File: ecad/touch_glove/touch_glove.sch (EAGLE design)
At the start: 173 parts, among them Q1 MCH3474 4A/30V, Q2 MCH3474 4A/30V, Q3 MCH3474 4A/30V, Q4 MCH3474 4A/30V, Q5 MCH3474 4A/30V, Q6 MCH3474 4A/30V, SW1 4A/28V, Y1 16 MHz

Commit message: Rev 2: Touch Glove.  Add op amps to flex sensor set 2.
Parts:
- removed ANT1: 2.45GHz, PiB_radio_frequency:ANTENNA_SMD_CHP-2.45GHZ-0.5DBI-3W
- removed D1: 1A/50V, PiB_discrete_semiconductors:DIODE_GENERAL-PURPOSE_SMD_GP_1A-50V
- removed Y1: 16 MHz, PiB:CRYSTAL_ABM3B_16MHZ_18PF
- added ANT: 2.45GHz, PiB_radio_frequency:ANTENNA_SMD_CHP-2.45GHZ-0.5DBI-3W
- added OPAMP1, OPAMP2, OPAMP3: LM358_DFN-EP, PiB_op_amps:LM358_DFN-EP
- added XTAL: 16 MHz, PiB:CRYSTAL_ABM3B_16MHZ_18PF
- C1, C2, C21, C3: value 100uF/16V -> 100uF/10V
- R1, R32, R33, R34, R35, R36, R37, R38, R39, R40, R41, R42, R43, R44, R45, R46, R47, R48: value 10KΩ -> 10K
- R10, R11, R12, R13, R14, R15, R6, R7, R8, R9: value 47K -> 10K; device PiB_resistors:47KΩ_SMD-0402_1/16W-5% -> PiB_resistors:10KΩ_SMD-0402_1/16W-5%
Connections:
- net A0 renamed SIG
- net PB6 renamed LED_RX
- net PB7 renamed LED_TX
- net PD4 renamed S0
- net PD5 renamed S1
- net PD6 renamed S3
- net PD7 renamed S2
- removed net A1: MCU.(ADC1/A1*)PF1
- removed net A2: MCU.(ADC2/DIG2/A2*)PF2
- removed net A3: MCU.(ADC3/DIG4/A3*)PF3
- removed net A4: MCU.(ADC4/TCK/A4*)PF4
- removed net A5: MCU.(ADC5/TMS/A5*)PF5
- removed net A6: MCU.(ADC6/TDO/A6*)PF6
- removed net A7: MCU.(ADC7/TDI/A7*)PF7
- removed net PB4: MCU.(PCINT4/OC2A/D9-PWM9)PB4
- removed net PB5: MCU.(PCINT5/OC1A/D8-PWM8)PB5
- removed net PE2: MCU.(XCK0/AIN0/D2)PE2
- removed net PE3: MCU.(AIN1/OC3A/D3-PWM3)PE3
- removed net PE4: MCU.(INT4/OC3B/D4-PWM4)PE4
- removed net PE5: MCU.(INT5/OC3C/D5-PWM5)PE5
- removed net PE6: MCU.(T3/INT6/D6)PE6
- removed net PE7: MCU.(ICP3/INT7/CLKO/D7)PE7
- removed net PG0: MCU.(DIG3/D16)PG0
- removed net PG1: MCU.(DIG1/D17)PG1
- removed net PG2: MCU.(AMR/D18)PG2
- removed net PG3: MCU.(TOSC2)PG3
- removed net PG4: MCU.(TOSC1)PG4
- removed net PG5: MCU.(OC0B/D19-PWM19)PG5
- removed net RX1: MCU.(INT2/RXD1/D20)PD2
- removed net SSN: MCU.(PCINT0/SSN/D10)PB0
- removed net TX1: MCU.(INT3/TXD1/D21)PD3
- removed net VBATT: C1.1, C2.1, C3.1, C4.1, C5.1, C6.1, C7.1, C8.1, C9.1, D1.K, D2.K, D3.K, LED1.A, SW1.S1, VREG-MCU.VIN, VREG-TEC.!SHDN, VREG-TEC.VIN, VREG-VIBE.VI
- new net N$10001: FLEX-PINKY2.-, OPAMP3.IN-A+, R15.2
- new net N$1004: FLEX-THUMB2.-, OPAMP1.IN-B+, R11.2
- new net N$38: FLEX-INDEX2.-, OPAMP1.IN-A+, R12.2
- new net N$41: FLEX-RING2.-, OPAMP2.IN-A+, R14.2
- new net N$991: FLEX-MIDDLE2.-, OPAMP2.IN-B+, R13.2
- new net VBAT: C1.1, C2.1, C3.1, C4.1, C5.1, C6.1, C7.1, C8.1, C9.1, D2.K, D3.K, LED1.A, SW1.S1, VREG-MCU.VIN, VREG-TEC.!SHDN, VREG-TEC.VIN, VREG-VIBE.VI
- net AGND: now also OPAMP1.V-, OPAMP2.V-, OPAMP3.V-
- net FLEX-INDEX2: now also OPAMP1.IN-A-, OPAMP1.OUT-A+; no longer FLEX-INDEX2.-, R12.2
- net FLEX-MIDDLE2: now also OPAMP2.IN-B-, OPAMP2.OUT-B; no longer FLEX-MIDDLE2.-, R13.2
- net FLEX-PINKY2: now also OPAMP3.IN-A-, OPAMP3.OUT-A+; no longer FLEX-PINKY2.-, R15.2
- net FLEX-RING2: now also OPAMP2.IN-A-, OPAMP2.OUT-A+; no longer FLEX-RING2.-, R14.2
- net FLEX-THUMB2: now also OPAMP1.IN-B-, OPAMP1.OUT-B; no longer FLEX-THUMB2.-, R11.2
- net N$35: now also XTAL.XTAL2; no longer Y1.XTAL2
- net N$36: now also XTAL.XTAL1; no longer Y1.XTAL1
- net RFSIG: now also ANT.SIGNAL; no longer ANT1.SIGNAL
- net VCC: no longer D1.A
- net VSENSOR: now also OPAMP1.V+, OPAMP2.V+, OPAMP3.V+
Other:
- note added: "LEDS"
- note added: "NEED 1.8V REGULATOR"
- note removed: "47K?"
- note removed: "A0/0 --> SIG_PIN of DEMUX"
- note removed: "D10"
- note removed: "D10 --> S3 of DEMUX"
- note removed: "D2"
- note removed: "D2 --> S0 of DEMUX"
- note removed: "D6"
- note removed: "D6 --> S1 of DEMUX"
- note removed: "D7"
- note removed: "D7 --> S2 of DEMUX"
- note removed: "I2C ADDR: x40"
- note removed: "Might add op amps"
- note removed: "TODO: LOTS OF VIAS"
- note removed: "TRY to change these pins?"
- note removed: "add diode CD1206-S01575"
- note removed: "deleted reset SW"
- note removed: "test"
- note removed: "was PE2"
- note removed: "was PE6"
- note removed: "was PE7"
- note removed: "was SSN"
- moved on the sheet: BALUN1, C1, C10, C11, C12, C13, C14, C15, C16, C17, C18, C19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

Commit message: Replaced supply devices from a non-existent library.
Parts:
- JP1: value JUMPER-SMT_3_NO_SILK -> JUMPER_SMD_3-PAD_NO_NO-SILK; device PiB_connectors:JUMPER-SMT_3_NO_SILK -> PiB_connectors:JUMPER_SMD_3-PAD_NO_NO-SILK
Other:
- note removed: "CHECK THESE FOR ACCURACY"

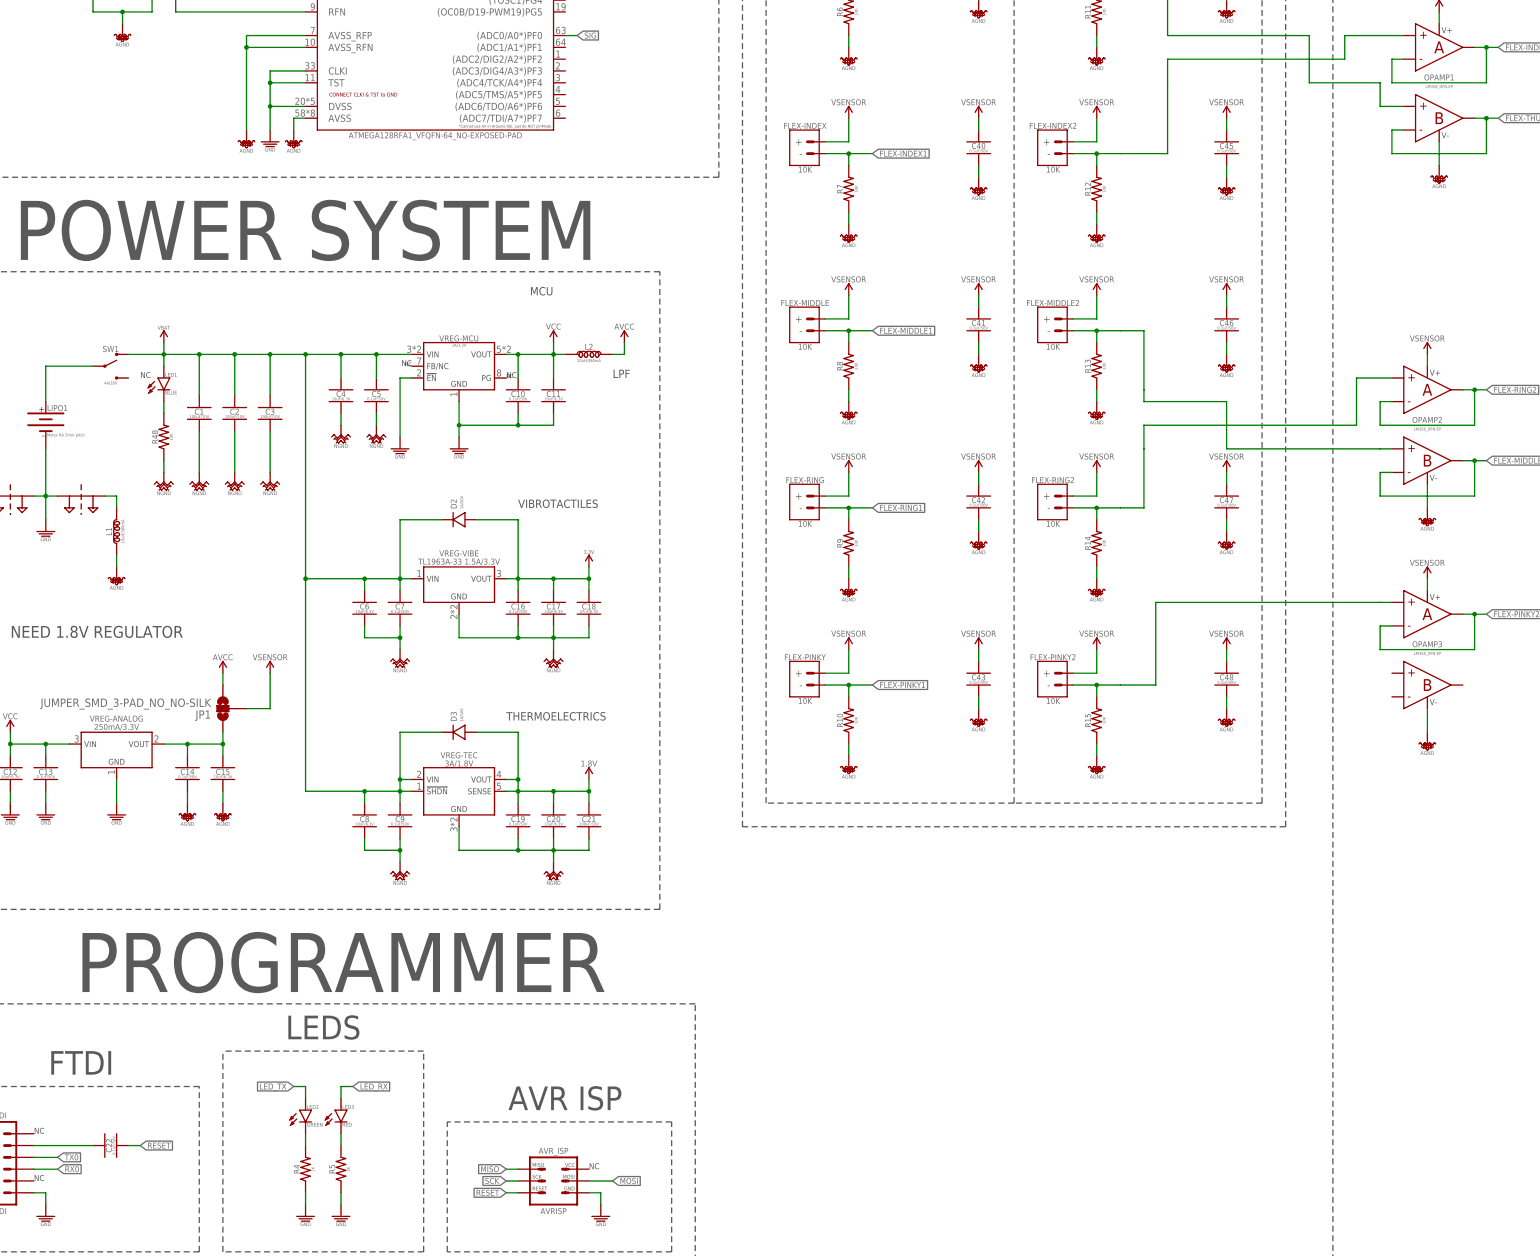
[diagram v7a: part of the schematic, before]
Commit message: Rev 2: Touch Glove.  Updated library meta data to reflect item availability.  Add 3D STEP file.
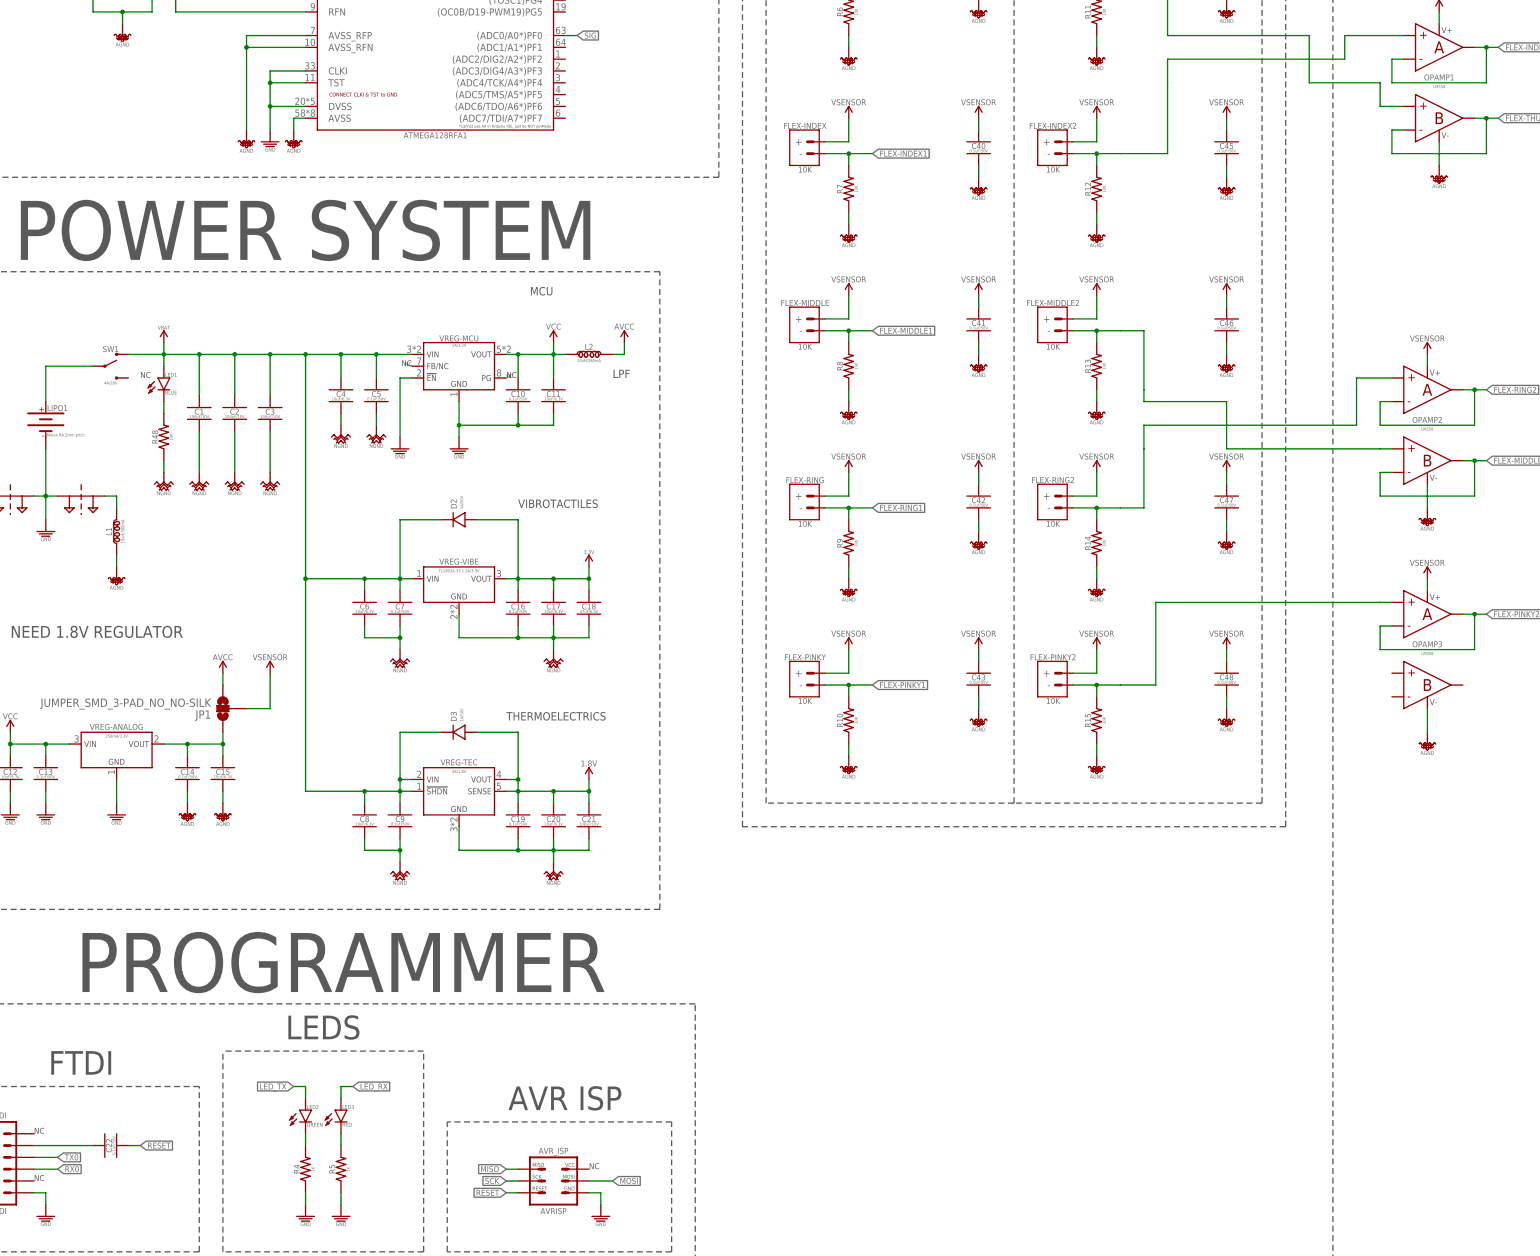
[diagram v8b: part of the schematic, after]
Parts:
- FLEX-INDEX, FLEX-MIDDLE, FLEX-PINKY, FLEX-RING, FLEX-THUMB: device PiB_sensors:FSR_FORCE-SENSATIVE-RESISTOR_PRESS-SENSOR_0530480210_RA-MALE_PITCH-1.25MM -> PiB_sensors:FLEX-SENSOR_0530480210_RA-MALE_PITCH-1.25MM
- FLEX-INDEX2, FLEX-MIDDLE2, FLEX-PINKY2, FLEX-RING2, FLEX-THUMB2: device PiB_sensors:FSR_FORCE-SENSATIVE-RESISTOR_PRESS-SENSOR_0530470210_VERT-MALE_PITCH-1.25MM -> PiB_sensors:FLEX-SENSOR_0530470210_VERT-MALE_PITCH-1.25MM
- JP2: value JUMPER-SMT_2_NO_SILK -> JUMPER_SMD_2-PAD_NO_SILK; device PiB_connectors:JUMPER-SMT_2_NO_SILK -> PiB_connectors:JUMPER_SMD_2-PAD_NO_SILK
- MCU: value ATMEGA128RFA1_VFQFN-64_NO-EXPOSED-PAD -> ATMEGA128RFA1; device PiB_ic_microcontrollers:ATMEGA128RFA1_VFQFN-64_NO-EXPOSED-PAD -> PiB_ic_microcontrollers:ATMEGA128RFA1_VFQFN-64_EXPOSED-PAD
- OPAMP1, OPAMP2, OPAMP3: value LM358_DFN-EP -> LM358
- R5: value 2K -> 1K; device PiB_resistors:2KΩ_SMD-0402_1/16W-5% -> PiB_resistors:1KΩ_SMD-0402_1/16W-5%
